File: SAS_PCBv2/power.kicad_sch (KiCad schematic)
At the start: 0 parts

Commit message: Power Input and LDO
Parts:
- added F1: Fuse, symbol Device:Fuse
- added J3: Conn_01x02_Pin, symbol Connector:Conn_01x02_Pin
- added SW1: SW_SPST, symbol Switch:SW_SPST
- added U2: SPX3819M5-L-3-3, Package_TO_SOT_SMD:SOT-23-5, symbol SAS_PCBv2_symbol:SPX3819M5-L-3-3
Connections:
- new net: F1.1, J3.1 (Pin_1)
- new net: F1.2, SW1.1 (A)
- new net +5V: SW1.2 (B)
- new net GND: J3.2 (Pin_2)
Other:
- note added: "5V power input XA current"
- note added: "Power Input"

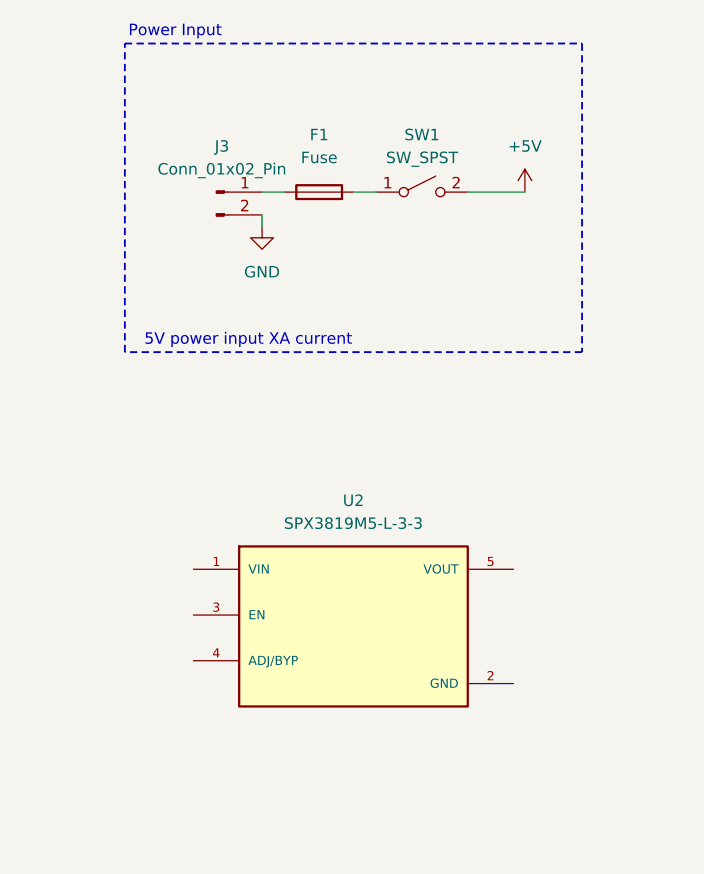
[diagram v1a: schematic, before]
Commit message: Added secondary displays, completed LDO 3V3
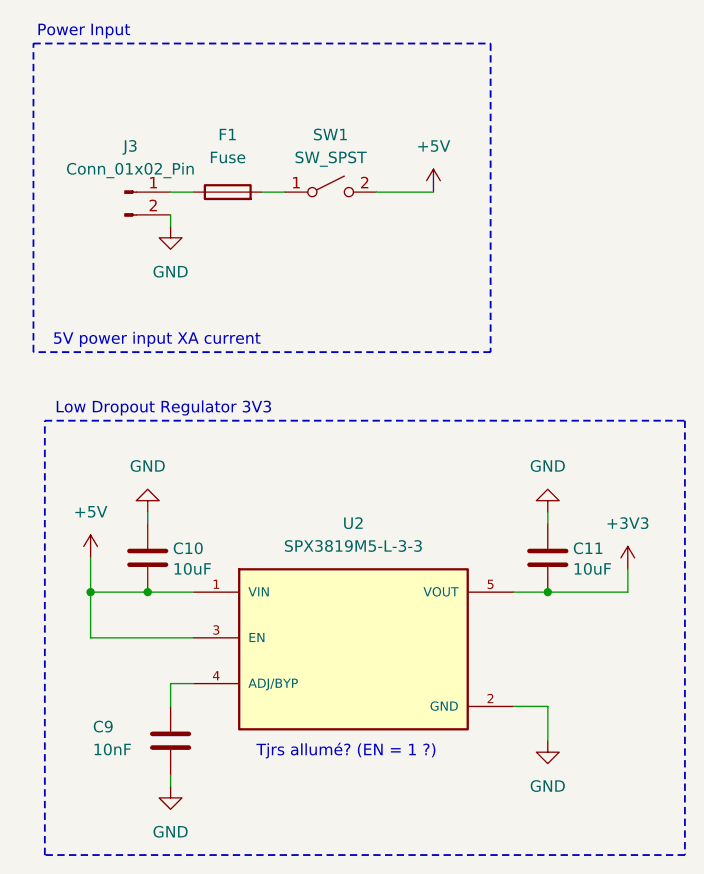
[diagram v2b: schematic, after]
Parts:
- added C10, C11: 10uF, symbol Device:C
- added C9: 10nF, symbol Device:C
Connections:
- net +5V: now also U2.1 (VIN), U2.3 (EN), C10.2
- net GND: now also U2.2 (GND), C10.1, C11.1, C9.2
- net at U2.4 (ADJ/BYP): now also C9.1
- net +3V3: now reaches U2.5 (VOUT)
- net +3V3: now also C11.2
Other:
- note added: "Low Dropout Regulator 3V3"
- note added: "Tjrs allumé? (EN = 1 ?)"
- moved on the sheet: F1, J3, SW1, U2

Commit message: debut buck
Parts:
- added MOD?: XL4015E Buck Module w/ Display, symbol Connector_Generic:Conn_02x02_Counter_Clockwise
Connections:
- net +5V: now also MOD?.4 (OUT+)
- net GND: now also MOD?.2 (IN-), MOD?.3 (OUT-)
- new net +7.5V: MOD?.1 (IN+)
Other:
- note added: "**Layout must include the 4 holes for the copper cylinders(screws). Follow measurements on the specs on the amazon page"
- note added: "Input V must be at least 1.5V higher than OUT"
- note added: "Warning: Module factory setting is HIGH VOLTAGE. DO NOT connect 5V loads (Raspberry Pi/Radio) yet. 1. Power on board. 2. Turn blue potentiometer CCW 7-15 turns. 3. Verify output is exactly 5.0V using the onboard LED display. 4. Power off, then connect 5V devices."

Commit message: schematic sans error et le debut de pcb
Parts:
- C10, C11: footprint (none) -> Capacitor_THT:CP_Radial_D5.0mm_P2.50mm
- C9: footprint (none) -> Capacitor_THT:C_Disc_D5.0mm_W2.5mm_P2.50mm
- F1: footprint (none) -> Fuse:Fuseholder_Cylinder-5x20mm_Schurter_0031_8201_Horizontal_Open
- J3: footprint (none) -> Connector_PinHeader_2.54mm:PinHeader_1x02_P2.54mm_Vertical
- MOD1: renamed from MOD?; footprint (none) -> SAS_PCBv2_footprint:XL4015E_Buck_Module_68x38mm(1)
- SW1: footprint (none) -> Button_Switch_THT:SW_DIP_SPSTx01_Piano_10.8x4.1mm_W7.62mm_P2.54mm
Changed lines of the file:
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@@
+	)
+	(junction
+		(at 147.32 49.53)
+		(diameter 0)
+		(color 0 0 0 0)
 	)
 	(junction
@@
 	)
 	(junction
+		(at 146.05 44.45)
+		(diameter 0)
+		(color 0 0 0 0)
+	)
+	(junction
 		(at 25.4 87.63)
 		(diameter 0)
@@
 		(on_board yes)
 		(dnp no)
-		(property "Reference" "MOD?"
+		(property "Reference" "MOD1"
 			(at 157.48 35.56 0)
 			(effects
@@
 			)
 		)
-		(property "Footprint" ""
+		(property "Footprint" "SAS_PCBv2_footprint:XL4015E_Buck_Module_68x38mm(1)"
 			(at 156.21 41.91 0)
 			(effects
@@
 			(project ""
 				(path "/9d66b581-dc57-43dc-b827-73e5c0cd12f6/3d73fe98-5b95-4bdf-b7ce-5bce46366f48"
-					(reference "MOD?")
+					(reference "MOD1")
 					(unit 1)
 				)
@@
 	)
 	(symbol
+		(lib_id "power:PWR_FLAG")
+		(at 147.32 49.53 90)
+		(unit 1)
+		(exclude_from_sim no)
+		(in_bom yes)
+		(on_board yes)
+		(dnp no)
+		(fields_autoplaced yes)
+		(property "Reference" "#FLG02"
+			(at 145.415 49.53 0)
+			(effects
+				(font
+					(size 1.27 1.27)
+				)
+				(hide yes)
+			)
+		)
+		(property "Value" "PWR_FLAG"
+			(at 143.51 49.5299 90)
+			(effects
+				(font
+					(size 1.27 1.27)
+				)
+				(justify left)
+			)
+		)
+		(property "Footprint" ""
+			(at 147.32 49.53 0)
+			(effects
+				(font
+					(size 1.27 1.27)
+				)
+				(hide yes)
+			)
+		)
+		(property "Datasheet" "~"
+			(at 147.32 49.53 0)
+			(effects
+				(font
+					(size 1.27 1.27)
+				)
+				(hide yes)
+			)
+		)
+		(property "Description" "Special symbol for telling ERC where power comes from"
+			(at 147.32 49.53 0)
+			(effects
+				(font
+					(size 1.27 1.27)
+				)
+				(hide yes)
+			)
+		)
+		(pin "1"
+		)
+		(instances
+			(project "SAS_PCBv2"
+				(path "/9d66b581-dc57-43dc-b827-73e5c0cd12f6/3d73fe98-5b95-4bdf-b7ce-5bce46366f48"
+					(reference "#FLG02")
+					(unit 1)
+				)
+			)
+		)
+	)
+	(symbol
 		(lib_id "Device:C")
 		(at 76.2 83.82 0)
@@
 			)
 		)
-		(property "Footprint" ""
+		(property "Footprint" "Capacitor_THT:CP_Radial_D5.0mm_P2.50mm"
 			(at 77.1652 87.63 0)
 			(effects
@@
 	)
 	(symbol
+		(lib_id "power:PWR_FLAG")
+		(at 146.05 44.45 90)
+		(unit 1)
+		(exclude_from_sim no)
+		(in_bom yes)
+		(on_board yes)
+		(dnp no)
+		(fields_autoplaced yes)
+		(property "Reference" "#FLG01"
+			(at 144.145 44.45 0)
+			(effects
+				(font
+					(size 1.27 1.27)
+				)
+				(hide yes)
+			)
+		)
+		(property "Value" "PWR_FLAG"
+			(at 142.24 44.4499 90)
+			(effects
+				(font
+					(size 1.27 1.27)
+				)
+				(justify left)
+			)
+		)
+		(property "Footprint" ""
+			(at 146.05 44.45 0)
+			(effects
+				(font
+					(size 1.27 1.27)
+				)
+				(hide yes)
+			)
+		)
+		(property "Datasheet" "~"
+			(at 146.05 44.45 0)
+			(effects
+				(font
+					(size 1.27 1.27)
+				)
+				(hide yes)
+			)
+		)
+		(property "Description" "Special symbol for telling ERC where power comes from"
+			(at 146.05 44.45 0)
+			(effects
+				(font
+					(size 1.27 1.27)
+				)
+				(hide yes)
+			)
+		)
+		(pin "1"
+		)
+		(instances
+			(project "SAS_PCBv2"
+				(path "/9d66b581-dc57-43dc-b827-73e5c0cd12f6/3d73fe98-5b95-4bdf-b7ce-5bce46366f48"
+					(reference "#FLG01")
+					(unit 1)
+				)
+			)
+		)
+	)
+	(symbol
 		(lib_id "Device:Fuse")
 		(at 40.64 43.18 90)
@@
 			)
 		)
-		(property "Footprint" ""
+		(property "Footprint" "Fuse:Fuseholder_Cylinder-5x20mm_Schurter_0031_8201_Horizontal_Open"
 			(at 40.64 44.958 90)
 			(effects
@@
 			)
 		)
-		(property "Footprint" ""
+		(property "Footprint" "Button_Switch_THT:SW_DIP_SPSTx01_Piano_10.8x4.1mm_W7.62mm_P2.54mm"
 			(at 52.07 43.18 0)
 			(effects
@@
 			)
 		)
-		(property "Footprint" ""
+		(property "Footprint" "Connector_PinHeader_2.54mm:PinHeader_1x02_P2.54mm_Vertical"
 			(at 29.21 43.18 0)
 			(effects
@@
 			)
 		)
-		(property "Footprint" ""
+		(property "Footprint" "Capacitor_THT:CP_Radial_D5.0mm_P2.50mm"
 			(at 32.7152 87.63 0)
 			(effects
@@
 			)
 		)
-		(property "Footprint" ""
+		(property "Footprint" "Capacitor_THT:C_Disc_D5.0mm_W2.5mm_P2.50mm"
 			(at 35.2552 107.95 0)
 			(effects

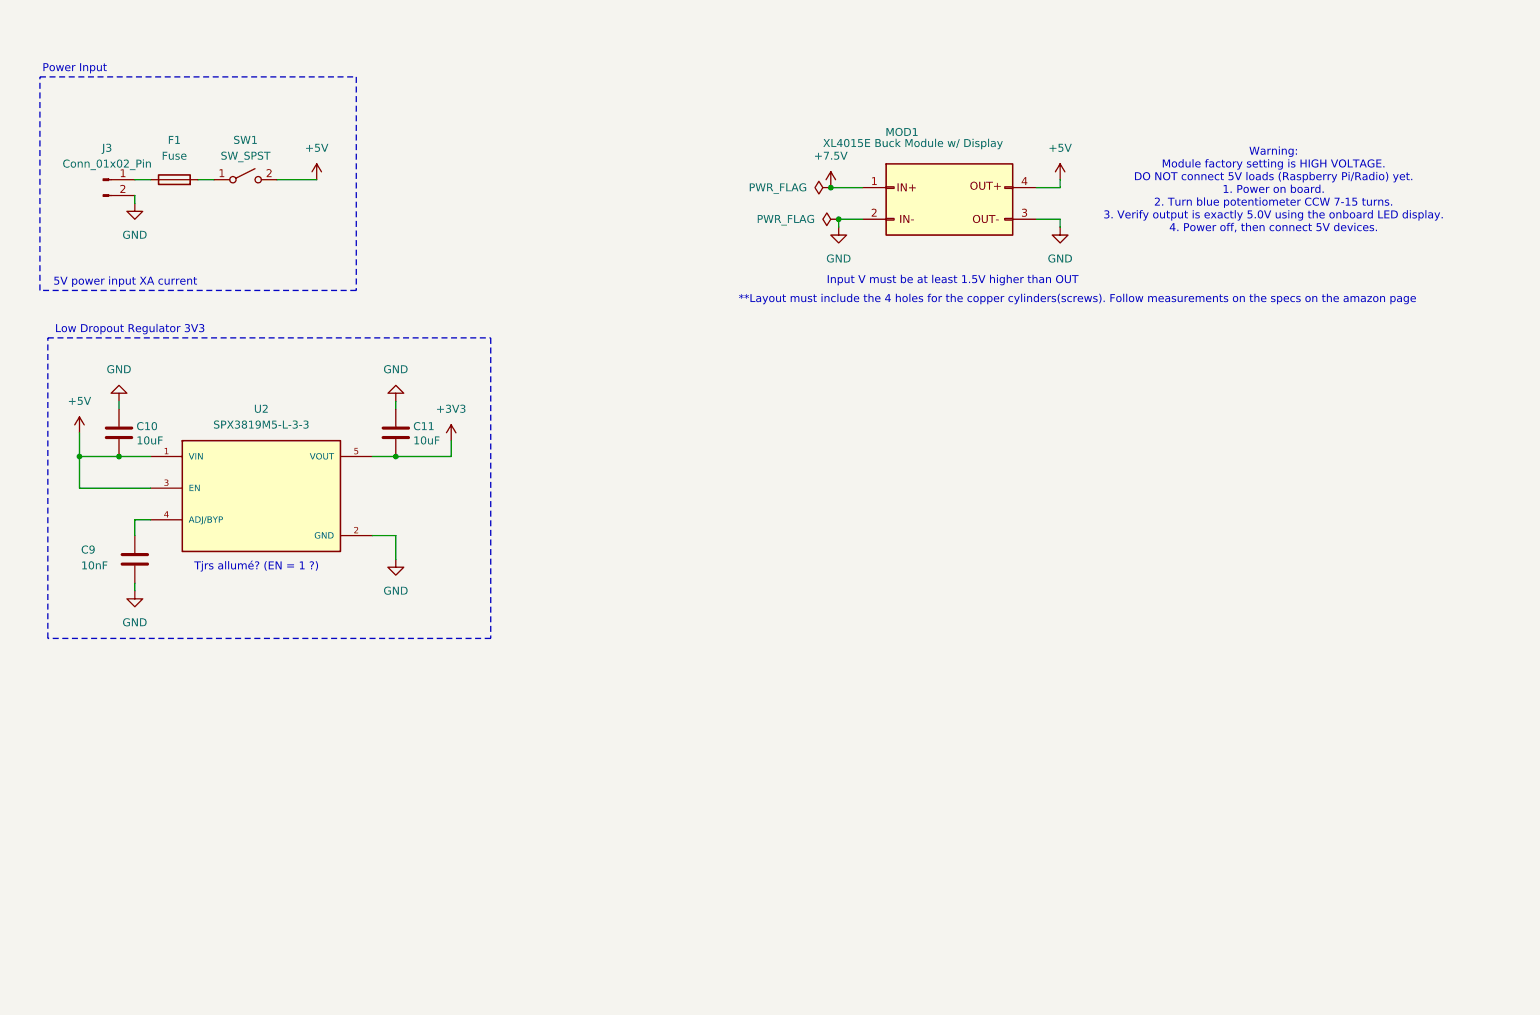
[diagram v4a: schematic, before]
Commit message: Switch USB/PCB, connections Power, spam condensateurs, resistance pull-up
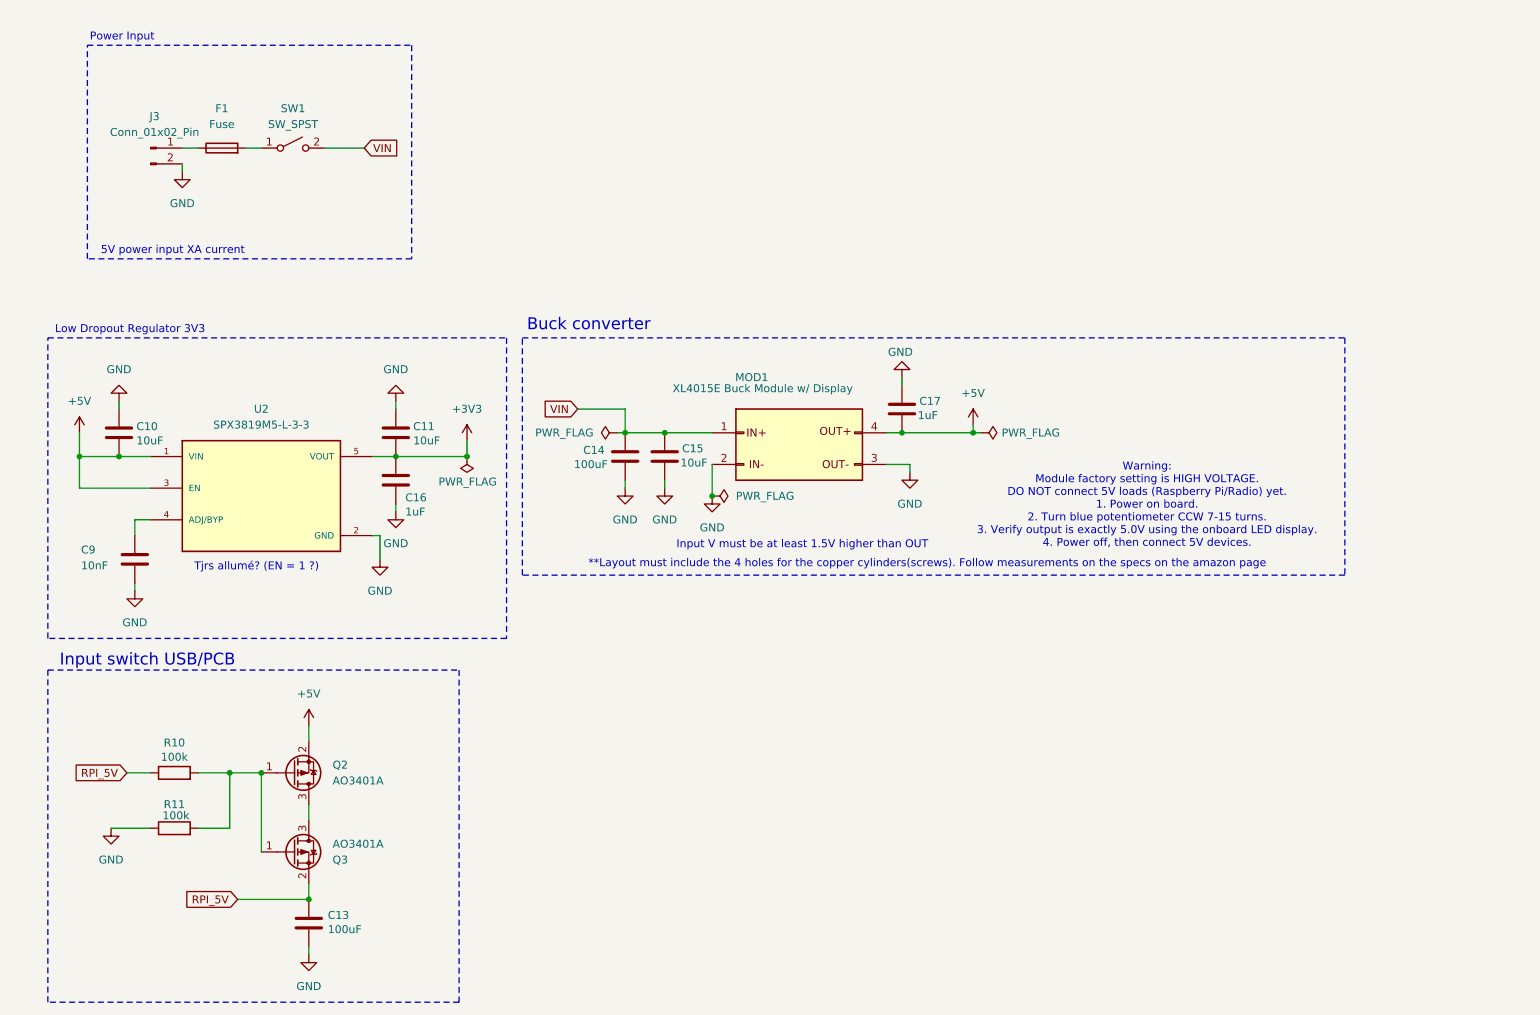
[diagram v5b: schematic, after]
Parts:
- added C13, C14: 100uF, symbol Device:C
- added C15: 10uF, symbol Device:C
- added C16: 1uF, Capacitor_THT:CP_Radial_D5.0mm_P2.50mm, symbol Device:C
- added C17: 1uF, symbol Device:C
- added Q2, Q3: AO3401A, Package_TO_SOT_SMD:SOT-23, symbol Transistor_FET:AO3401A
- added R10, R11: 100k, symbol Device:R
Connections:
- net +3V3: now also C16.1
- net +5V: now also C17.2, Q2.2 (S); no longer SW1.2 (B)
- net GND: now also C13.2, C14.2, C15.2, C16.2, C17.1, R11.1
- net +7.5V renamed VIN
- net VIN: now also SW1.2 (B), C14.1, C15.1
- new net: Q2.1 (G), Q3.1 (G), R10.2, R11.2
- new net: Q2.3 (D), Q3.3 (D)
- new net RPI_5V: C13.1, Q3.2 (S), R10.1
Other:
- note added: "Buck converter"
- note added: "Input switch USB/PCB"
- moved on the sheet: F1, J3, MOD1, SW1

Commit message: LDO du service, Logic level shifter custom
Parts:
- removed C11: 10uF, Capacitor_THT:CP_Radial_D5.0mm_P2.50mm, symbol Device:C
- removed C16: 1uF, Capacitor_THT:CP_Radial_D5.0mm_P2.50mm, symbol Device:C
- removed U2: SPX3819M5-L-3-3, Package_TO_SOT_SMD:SOT-23-5, symbol SAS_PCBv2_symbol:SPX3819M5-L-3-3
- added U2: LF33_TO220, Package_TO_SOT_THT:TO-220-3_Vertical, symbol Regulator_Linear:LF33_TO220
- C10: value 10uF -> 2.2uF; footprint Capacitor_THT:CP_Radial_D5.0mm_P2.50mm -> SAS_PCBv2_footprint:CAP_FG14_TDK
- C9: value 10nF -> 0.1uF; footprint Capacitor_THT:C_Disc_D5.0mm_W2.5mm_P2.50mm -> SAS_PCBv2_footprint:CAP_C320_KEM
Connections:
- net +3V3: now also C10.1, U2.3 (VO)
- net +5V: now also C9.1, U2.1 (VI); no longer C10.2
- net GND: now also C10.2, U2.2 (GND); no longer C10.1
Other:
- note removed: "Tjrs allumé? (EN = 1 ?)"
